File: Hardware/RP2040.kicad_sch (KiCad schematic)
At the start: 27 parts, among them U1 W25Q128JVS, U2 RP2040, Y1 ABM8-272-T3

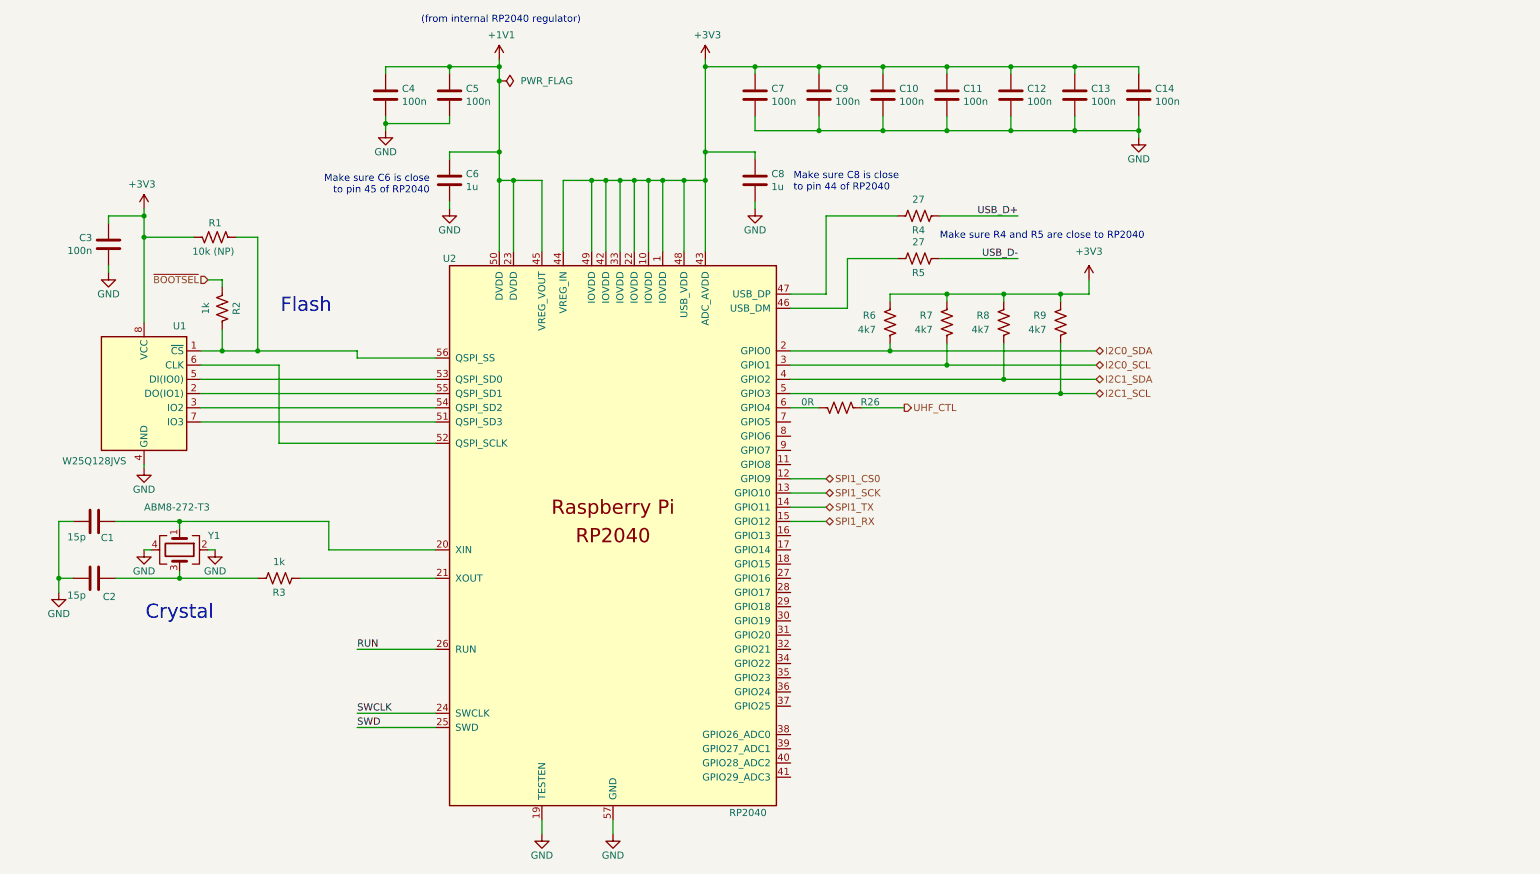
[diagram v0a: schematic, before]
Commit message: Add RP2040 SWD
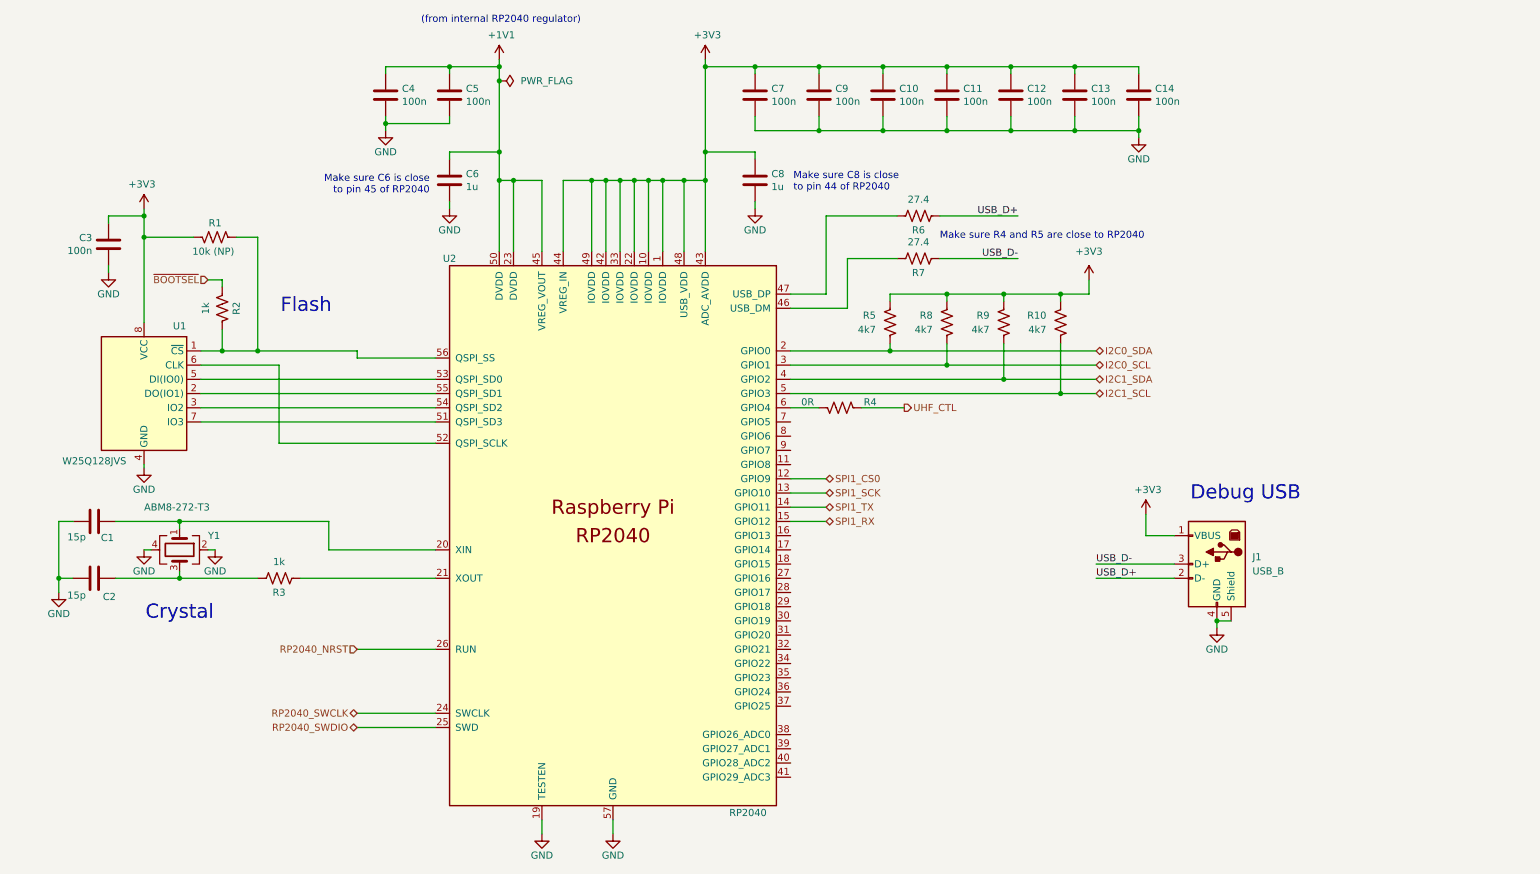
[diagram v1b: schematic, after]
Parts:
- added J1: USB_B, symbol Connector:USB_B
- R6: renamed from R4; value 27 -> 27.4
- R7: renamed from R5; value 27 -> 27.4
- renumbered R9 to R10, R26 to R4, R6 to R5, R7 to R8, R8 to R9
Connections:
- net +3V3: now also J1.1 (VBUS)
- net GND: now also J1.4 (GND), J1.5 (Shield)
- net USB_D+: now also J1.2 (D-)
- net USB_D-: now also J1.3 (D+)
- net RUN renamed RP2040_NRST
- net SWCLK renamed RP2040_SWCLK
- net SWD renamed RP2040_SWDIO
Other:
- note added: "Debug USB"

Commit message: Finish schematic v1
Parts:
- added J24: 2-Pin Header, symbol Connector_Generic:Conn_02x01
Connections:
- net +3V3: now also J24.1 (Pin_1); no longer J1.1 (VBUS)
- new net: J1.1 (VBUS), J24.2 (Pin_2)
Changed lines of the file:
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@@
 	)
 	(junction
-		(at 186.69 64.77)
-		(diameter 0)
-		(color 0 0 0 0)
-	)
-	(junction
 		(at 256.54 113.03)
 		(diameter 0)
@@
 	(wire
 		(pts
-			(xy 302.26 146.05) (xy 307.34 146.05)
-		)
-		(stroke
-			(width 0)
-			(type default)
-		)
-	)
-	(wire
-		(pts
 			(xy 161.29 113.03) (xy 161.29 114.3)
 		)
@@
 	(wire
 		(pts
-			(xy 186.69 62.23) (xy 186.69 64.77)
+			(xy 186.69 62.23) (xy 186.69 77.47)
 		)
 		(stroke
@@
 	(wire
 		(pts
-			(xy 186.69 64.77) (xy 186.69 77.47)
-		)
-		(stroke
-			(width 0)
-			(type default)
-		)
-	)
-	(wire
-		(pts
 			(xy 266.7 73.66) (xy 255.27 73.66)
 		)
@@
 	(wire
 		(pts
-			(xy 302.26 142.24) (xy 302.26 146.05)
-		)
-		(stroke
-			(width 0)
-			(type default)
-		)
-	)
-	(wire
-		(pts
 			(xy 166.37 63.5) (xy 166.37 62.23)
 		)
@@
 	(symbol
 		(lib_id "power:+3V3")
-		(at 302.26 142.24 0)
+		(at 294.64 146.05 90)
+		(mirror x)
 		(unit 1)
 		(exclude_from_sim no)
@@
 		(on_board yes)
 		(dnp no)
+		(fields_autoplaced yes)
 		(property "Reference" "#PWR016"
-			(at 302.26 146.05 0)
+			(at 298.45 146.05 0)
 			(effects
 				(font
@@
 		)
 		(property "Value" "+3V3"
-			(at 302.641 137.8458 0)
+			(at 290.83 146.0501 90)
 			(effects
 				(font
 					(size 1.27 1.27)
 				)
+				(justify left)
 			)
 		)
 		(property "Footprint" ""
-			(at 302.26 142.24 0)
+			(at 294.64 146.05 0)
 			(effects
 				(font
@@
 		)
 		(property "Datasheet" ""
-			(at 302.26 142.24 0)
+			(at 294.64 146.05 0)
 			(effects
 				(font
@@
 			)
 		)
-		(property "Description" ""
-			(at 302.26 142.24 0)
+		(property "Description" "Power symbol creates a global label with name \"+3V3\""
+			(at 294.64 146.05 0)
 			(effects
 				(font
 					(size 1.27 1.27)
 				)
+				(hide yes)
 			)
 		)
@@
 	)
 	(symbol
-		(lib_id "power:PWR_FLAG")
-		(at 186.69 64.77 270)
-		(unit 1)
-		(exclude_from_sim no)
-		(in_bom yes)
-		(on_board yes)
-		(dnp no)
-		(fields_autoplaced yes)
-		(property "Reference" "#FLG01"
-			(at 188.595 64.77 0)
-			(effects
-				(font
-					(size 1.27 1.27)
-				)
-				(hide yes)
-			)
-		)
-		(property "Value" "PWR_FLAG"
-			(at 190.5 64.7699 90)
-			(effects
-				(font
-					(size 1.27 1.27)
-				)
-				(justify left)
-			)
-		)
-		(property "Footprint" ""
-			(at 186.69 64.77 0)
-			(effects
-				(font
-					(size 1.27 1.27)
-				)
-				(hide yes)
-			)
-		)
-		(property "Datasheet" "~"
-			(at 186.69 64.77 0)
-			(effects
-				(font
-					(size 1.27 1.27)
-				)
-				(hide yes)
-			)
-		)
-		(property "Description" "Special symbol for telling ERC where power comes from"
-			(at 186.69 64.77 0)
-			(effects
-				(font
-					(size 1.27 1.27)
-				)
-				(hide yes)
-			)
-		)
-		(pin "1"
-		)
-		(instances
-			(project ""
-				(path "/58243925-df8d-4fc1-899e-fce866d1d25a/bec95c26-e44f-4f6a-97be-aee51e3bba5a"
-					(reference "#FLG01")
-					(unit 1)
-				)
-			)
-		)
-	)
-	(symbol
 		(lib_id "Device:R_US")
 		(at 147.32 153.67 270)
@@
 					(unit 1)
 				)
+			)
+		)
+	)
+	(symbol
+		(lib_id "Connector_Generic:Conn_02x01")
+		(at 299.72 146.05 0)
+		(unit 1)
+		(exclude_from_sim no)
+		(in_bom yes)
+		(on_board yes)
+		(dnp no)
+		(property "Reference" "J24"
+			(at 300.99 140.716 0)
+			(effects
+				(font
+					(size 1.27 1.27)
+				)
+			)
+		)
+		(property "Value" "2-Pin Header"
+			(at 300.99 143.256 0)
+			(effects
+				(font
+					(size 1.27 1.27)
+				)
+			)
+		)
+		(property "Footprint" ""
+			(at 299.72 146.05 0)
+			(effects
+				(font
+					(size 1.27 1.27)
+				)
+				(hide yes)
+			)
+		)
+		(property "Datasheet" "~"
+			(at 299.72 146.05 0)
+			(effects
+				(font
+					(size 1.27 1.27)
+				)
+				(hide yes)
+			)
+		)
+		(property "Description" "Generic connector, double row, 02x01, this symbol is compatible with counter-clockwise, top-bottom and odd-even numbering schemes., script generated (kicad-library-utils/schlib/autogen/connector/)"
+			(at 299.72 146.05 0)
+			(effects
+				(font
+					(size 1.27 1.27)
+				)
+				(hide yes)
+			)
+		)
+		(pin "1"
+		)
+		(pin "2"
+		)
+		(instances
+			(project "CTS-SAT-2-OBC-PCB"
+				(path "/58243925-df8d-4fc1-899e-fce866d1d25a/bec95c26-e44f-4f6a-97be-aee51e3bba5a"
+					(reference "J24")
+					(unit 1)
+				)

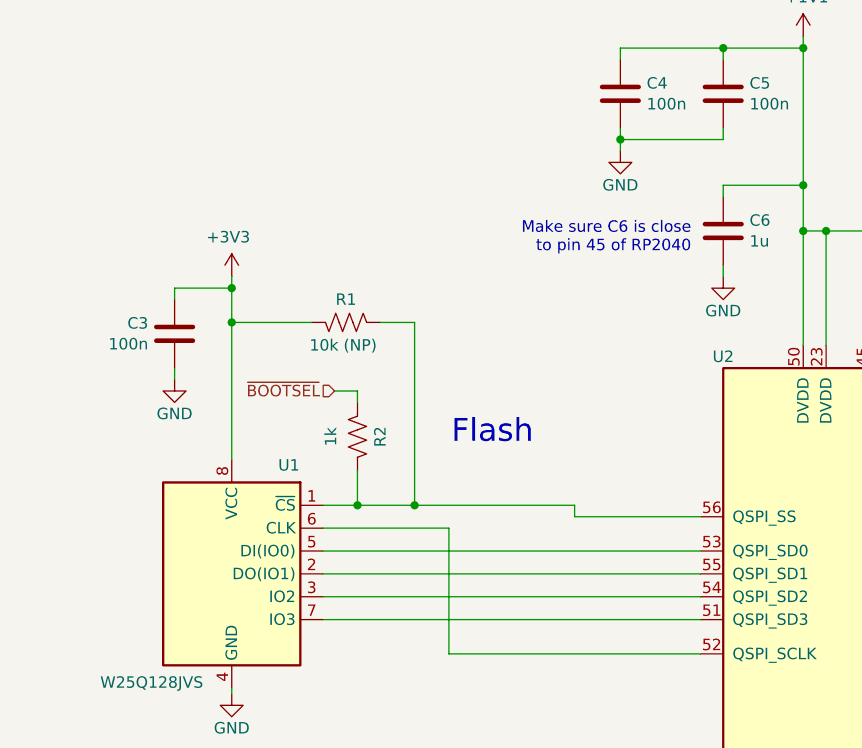
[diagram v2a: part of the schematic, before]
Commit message: Fix RP2040 BOOTSEL
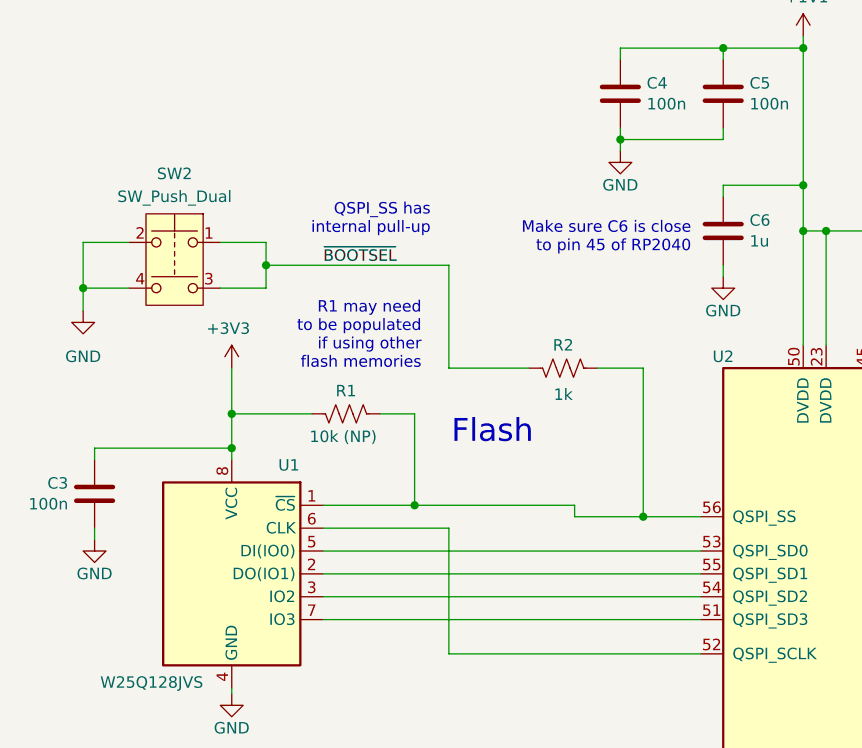
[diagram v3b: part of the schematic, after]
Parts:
- added SW2: SW_Push_Dual, symbol Switch:SW_Push_Dual
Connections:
- net GND: now also SW2.2, SW2.4
- net ~{BOOTSEL}: now also SW2.1, SW2.3
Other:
- note added: "QSPI_SS has internal pull-up"
- note added: "R1 may need to be populated if using other flash memories"
- moved on the sheet: C3, R1, R2

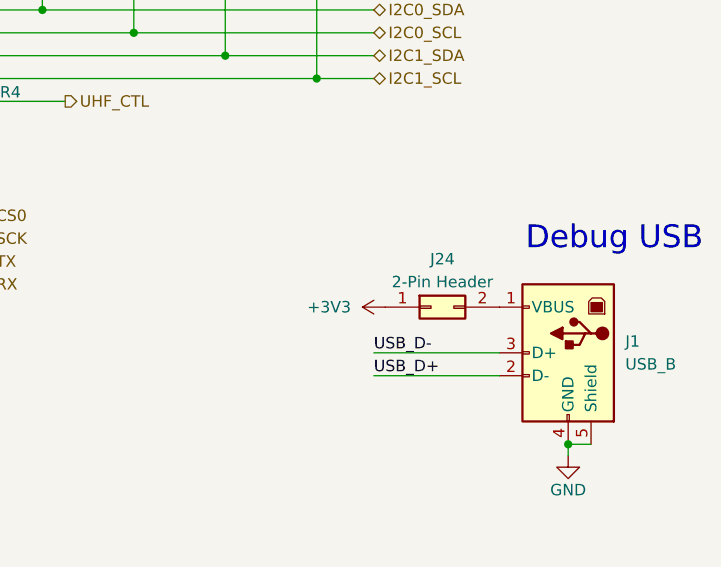
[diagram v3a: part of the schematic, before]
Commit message: Assign footprints
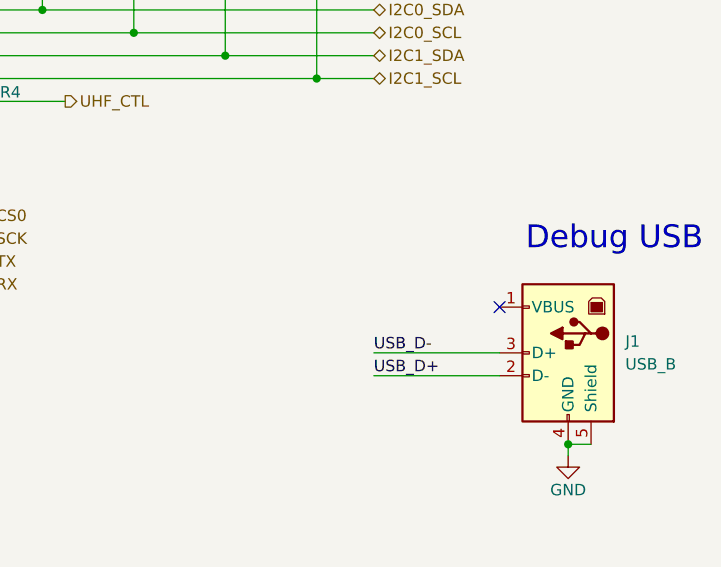
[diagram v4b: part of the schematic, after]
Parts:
- removed J24: 2-Pin Header, symbol Connector_Generic:Conn_02x01
- R10, R4, R5, R8, R9: footprint (none) -> Resistor_SMD:R_0603_1608Metric
- SW2: footprint (none) -> PTS526:SMT_FS
- U1: footprint Package_SO:SOIC-8_5.23x5.23mm_P1.27mm -> W25Q128JVS:SOIC-8_5.23x5.23mm_P1.27mm
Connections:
- no-connect marks 0 -> 1
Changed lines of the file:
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@@
 		(color 0 0 0 0)
 	)
+	(no_connect
+		(at 307.34 146.05)
+	)
 	(wire
 		(pts
@@
 			)
 		)
-		(property "Footprint" ""
+		(property "Footprint" "Resistor_SMD:R_0603_1608Metric"
 			(at 275.844 108.204 90)
 			(effects
@@
 	)
 	(symbol
-		(lib_id "power:+3V3")
-		(at 294.64 146.05 90)
-		(mirror x)
-		(unit 1)
-		(exclude_from_sim no)
-		(in_bom yes)
-		(on_board yes)
-		(dnp no)
-		(fields_autoplaced yes)
-		(property "Reference" "#PWR016"
-			(at 298.45 146.05 0)
-			(effects
-				(font
-					(size 1.27 1.27)
-				)
-				(hide yes)
-			)
-		)
-		(property "Value" "+3V3"
-			(at 290.83 146.0501 90)
-			(effects
-				(font
-					(size 1.27 1.27)
-				)
-				(justify left)
-			)
-		)
-		(property "Footprint" ""
-			(at 294.64 146.05 0)
-			(effects
-				(font
-					(size 1.27 1.27)
-				)
-				(hide yes)
-			)
-		)
-		(property "Datasheet" ""
-			(at 294.64 146.05 0)
-			(effects
-				(font
-					(size 1.27 1.27)
-				)
-				(hide yes)
-			)
-		)
-		(property "Description" "Power symbol creates a global label with name \"+3V3\""
-			(at 294.64 146.05 0)
-			(effects
-				(font
-					(size 1.27 1.27)
-				)
-				(hide yes)
-			)
-		)
-		(pin "1"
-		)
-		(instances
-			(project "CTS-SAT-2-OBC-PCB"
-				(path "/58243925-df8d-4fc1-899e-fce866d1d25a/bec95c26-e44f-4f6a-97be-aee51e3bba5a"
-					(reference "#PWR016")
-					(unit 1)
-				)
-			)
-		)
-	)
-	(symbol
 		(lib_id "Device:Crystal_GND24")
 		(at 129.54 148.59 270)
@@
 			)
 		)
-		(property "Footprint" "Package_SO:SOIC-8_5.23x5.23mm_P1.27mm"
+		(property "Footprint" "W25Q128JVS:SOIC-8_5.23x5.23mm_P1.27mm"
 			(at 123.19 120.65 0)
 			(effects
@@
 			)
 		)
-		(property "Footprint" ""
+		(property "Footprint" "Resistor_SMD:R_0603_1608Metric"
 			(at 286.004 108.204 90)
 			(effects
@@
 			)
 		)
-		(property "Footprint" ""
+		(property "Footprint" "Resistor_SMD:R_0603_1608Metric"
 			(at 247.396 122.174 90)
 			(effects
@@
 			)
 		)
-		(property "Footprint" ""
+		(property "Footprint" "Resistor_SMD:R_0603_1608Metric"
 			(at 255.524 108.204 90)
 			(effects
@@
 			)
 		)
-		(property "Footprint" ""
+		(property "Footprint" "Resistor_SMD:R_0603_1608Metric"
 			(at 265.684 108.204 90)
 			(effects
@@
 	)
 	(symbol
-		(lib_id "Connector_Generic:Conn_02x01")
-		(at 299.72 146.05 0)
-		(unit 1)
-		(exclude_from_sim no)
-		(in_bom yes)
-		(on_board yes)
-		(dnp no)
-		(property "Reference" "J24"
-			(at 300.99 140.716 0)
-			(effects
-				(font
-					(size 1.27 1.27)
-				)
-			)
-		)
-		(property "Value" "2-Pin Header"
-			(at 300.99 143.256 0)
-			(effects
-				(font
-					(size 1.27 1.27)
-				)
-			)
-		)
-		(property "Footprint" ""
-			(at 299.72 146.05 0)
-			(effects
-				(font
-					(size 1.27 1.27)
-				)
-				(hide yes)
-			)
-		)
-		(property "Datasheet" "~"
-			(at 299.72 146.05 0)
-			(effects
-				(font
-					(size 1.27 1.27)
-				)
-				(hide yes)
-			)
-		)
-		(property "Description" "Generic connector, double row, 02x01, this symbol is compatible with counter-clockwise, top-bottom and odd-even numbering schemes., script generated (kicad-library-utils/schlib/autogen/connector/)"
-			(at 299.72 146.05 0)
-			(effects
-				(font
-					(size 1.27 1.27)
-				)
-				(hide yes)
-			)
-		)
-		(pin "1"
-		)
-		(pin "2"
-		)
-		(instances
-			(project "CTS-SAT-2-OBC-PCB"
-				(path "/58243925-df8d-4fc1-899e-fce866d1d25a/bec95c26-e44f-4f6a-97be-aee51e3bba5a"
-					(reference "J24")
-					(unit 1)
-				)
-			)
-		)
-	)
-	(symbol
 		(lib_id "power:GND")
 		(at 166.37 73.66 0)
@@
 			)
 		)
-		(property "Footprint" ""
+		(property "Footprint" "PTS526:SMT_FS"
 			(at 116.84 78.74 0)
 			(effects
